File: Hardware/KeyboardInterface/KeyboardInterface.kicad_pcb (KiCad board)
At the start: 2 copper layers, 49 x 49 mm, 10 parts, among them J1 PS/2, J2 CIA, J3 POWER, U1 74HC14, U2 74HC595, U3 74HC595

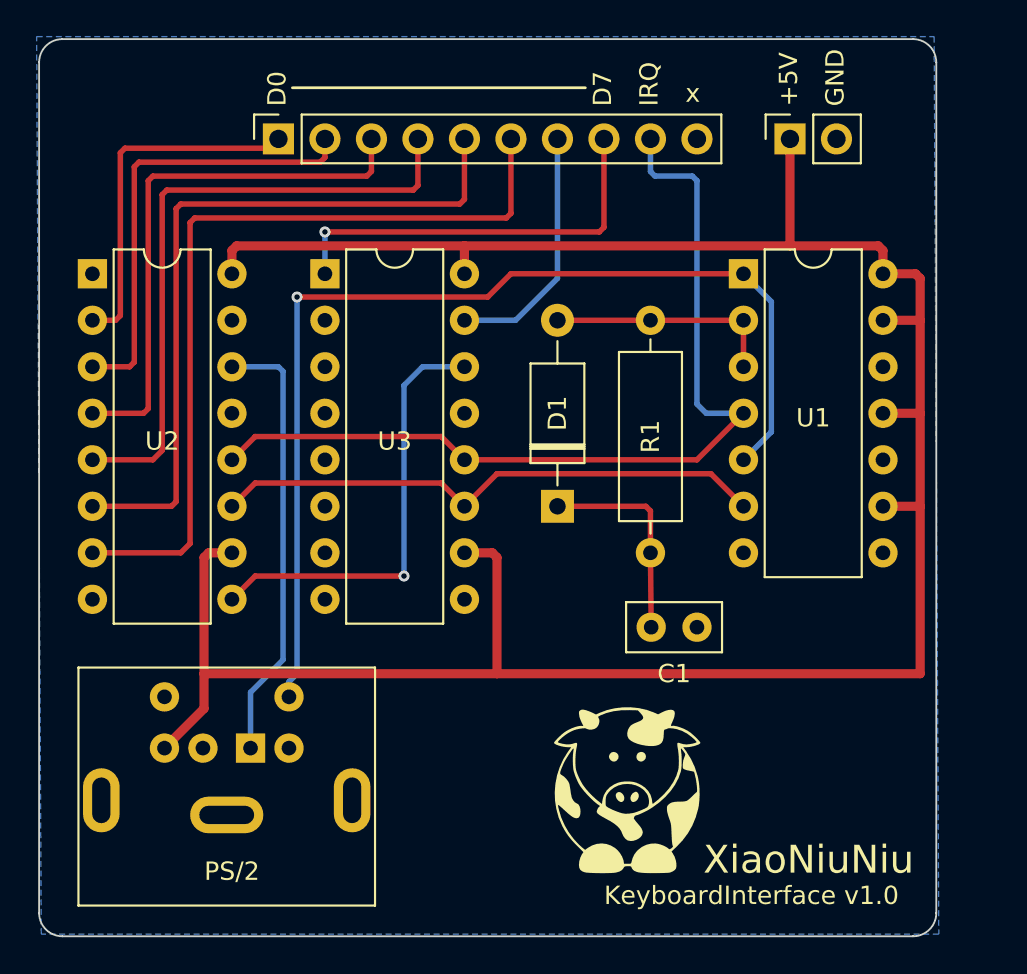
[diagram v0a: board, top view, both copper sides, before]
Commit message: Serial Software
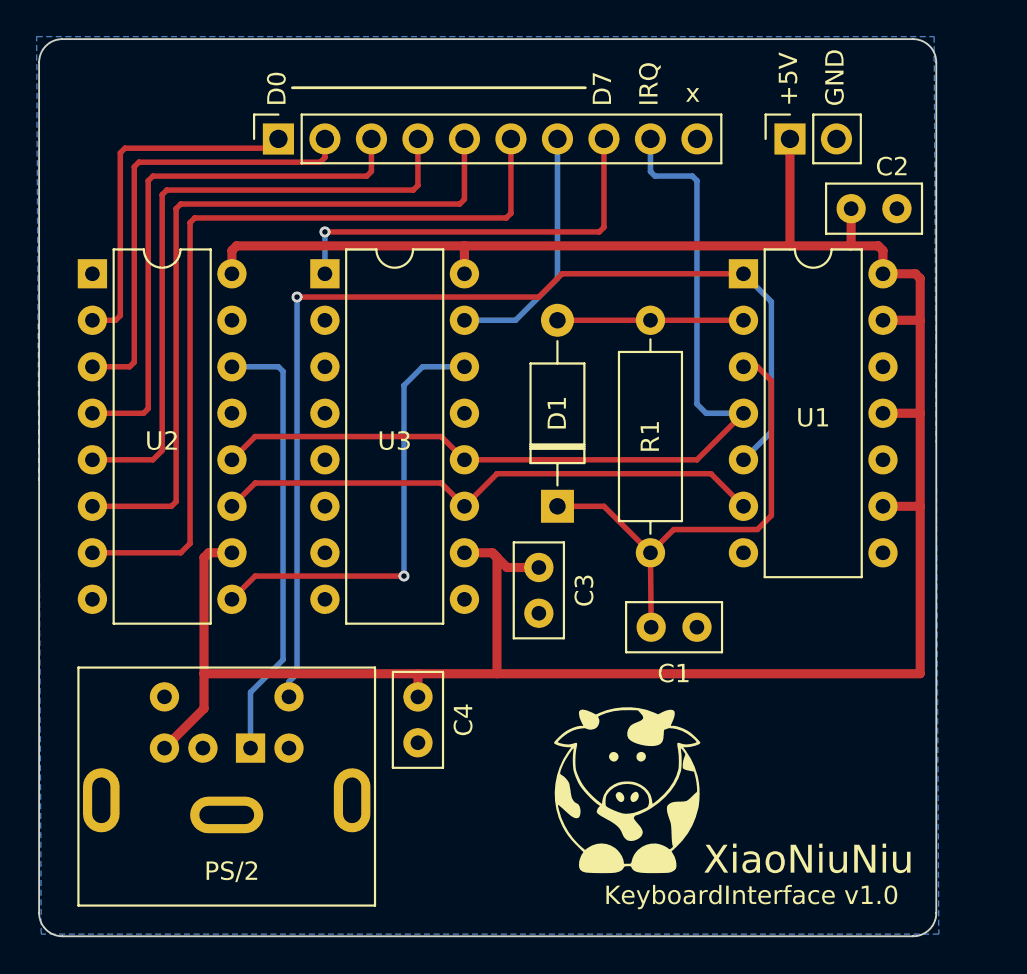
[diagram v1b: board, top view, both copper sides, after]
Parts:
- added C2: 100nF, Capacitor_THT:C_Disc_D5.0mm_W2.5mm_P2.50mm, F.Cu at (117.6, 59.7)
- added C3: 100nF, Capacitor_THT:C_Disc_D5.0mm_W2.5mm_P2.50mm, F.Cu at (100.6, 79.3)
- added C4: 100nF, Capacitor_THT:C_Disc_D5.0mm_W2.5mm_P2.50mm, F.Cu at (94.0, 86.4)
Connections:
- U1 pad 3: Net-(D1-A) -> Net-(D1-K)
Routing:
- net Net-(D1-K): track 11.5 -> 26.8 mm
- net +5V: track 135.8 -> 142.0 mm
- net Net-(D1-A): track 12.7 -> 10.2 mm
